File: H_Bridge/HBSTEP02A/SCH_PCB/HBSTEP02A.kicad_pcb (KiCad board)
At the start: 2 copper layers, 0 parts

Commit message: nakresleno schema. Vygenerovan netlist a zalozen PCB.
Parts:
- added C1: 4u7, Capacitors_SMD:C_0805, F.Cu at (188.0, 92.0)
- added C10: 22n, Capacitors_SMD:C_0805, F.Cu at (187.1, 110.9)
- added C11: 100nF, Capacitors_SMD:C_0805, F.Cu at (192.0, 107.3)
- added C12: 470nF, Capacitors_SMD:C_0805, F.Cu at (196.8, 113.6)
- added C13: 100nF, Capacitors_SMD:C_0805, F.Cu at (183.6, 123.5)
- added C14: 100nF, Capacitors_SMD:C_0805, F.Cu at (202.3, 107.3)
- added C15: 470pF, Capacitors_SMD:C_0805, F.Cu at (191.7, 113.6)
- added C16: 470pF, Capacitors_SMD:C_0805, F.Cu at (197.1, 107.3)
- added C17: 470pF, Capacitors_SMD:C_0805, F.Cu at (186.1, 117.2)
- added C18: 470pF, Capacitors_SMD:C_0805, F.Cu at (202.6, 101.0)
- added C19: 4n7, Capacitors_SMD:C_0805, F.Cu at (179.0, 121.3)
- added C2: 100nF, Capacitors_SMD:C_0805, F.Cu at (202.2, 81.6)
- added C20: 4n7, Capacitors_SMD:C_0805, F.Cu at (204.9, 94.2)
- added C21: 4n7, Capacitors_SMD:C_0805, F.Cu at (190.7, 119.9)
- added C22: 4n7, Capacitors_SMD:C_0805, F.Cu at (195.4, 88.4)
- added C3: 100nF, Capacitors_SMD:C_0805, F.Cu at (200.0, 88.4)
- added C4: 100nF, Capacitors_SMD:C_0805, F.Cu at (188.5, 98.3)
- added C5: 100nF, Capacitors_SMD:C_0805, F.Cu at (178.8, 108.0)
- added C6: 4u7, Capacitors_SMD:C_0805, F.Cu at (170.1, 114.8)
- added C7: 100uF/50V, Capacitors_ThroughHole:C_Radial_D10_L13_P5, F.Cu at (161.2, 75.3)
- added C8: 1nF, Capacitors_SMD:C_0805, F.Cu at (164.0, 125.0)
- added C9: 1nF, Capacitors_SMD:C_0805, F.Cu at (174.1, 114.8)
- added D1: M4, Diodes_SMD:SMA_Handsoldering, F.Cu at (136.7, 122.2)
- added D2: MSS1P6, HBSTEP02A:SCHOT_D_MSS1P6, F.Cu at (173.0, 108.7)
- added D3: MSS1P6, HBSTEP02A:SCHOT_D_MSS1P6, F.Cu at (166.5, 108.7)
- added D4: MSS1P6, HBSTEP02A:SCHOT_D_MSS1P6, F.Cu at (158.7, 123.4)
- added D5: MSS1P6, HBSTEP02A:SCHOT_D_MSS1P6, F.Cu at (178.8, 101.9)
- added J1: VIO 3.3-5V, Mlab_Pin_Headers:Straight_2x03, F.Cu at (125.3, 114.4)
- added J10: SDO/NAO/CFG0, Mlab_Pin_Headers:Straight_1x02, F.Cu at (130.9, 73.2)
- added J11: ENCN/DCO, Mlab_Pin_Headers:Straight_1x02, F.Cu at (156.1, 98.3)
- added J12: ENCB/DCEN/CFG4, Mlab_Pin_Headers:Straight_1x02, F.Cu at (111.1, 73.2)
- added J13: ENCA/DCIN/CFG5, Mlab_Pin_Headers:Straight_1x02, F.Cu at (110.7, 83.6)
- added J14: SWP/DIAG1, Mlab_Pin_Headers:Straight_1x02, F.Cu at (138.5, 113.1)
- added J15: SWN/DIAG0, Mlab_Pin_Headers:Straight_1x02, F.Cu at (162.9, 87.9)
- added J16: CONN1_1, Mlab_Con:WAGO256, F.Cu at (108.2, 99.8)
- added J17: CONN1_1, Mlab_Con:WAGO256, F.Cu at (128.6, 81.1)
- added J18: POWER SELECT, Mlab_Pin_Headers:Straight_1x03, F.Cu at (127.2, 101.4)
- added J19: SDMODE, Mlab_Pin_Headers:Straight_1x02, F.Cu at (181.1, 94.0)
- added J2: REFL/STEP, Mlab_Pin_Headers:Straight_1x02, F.Cu at (175.6, 73.2)
- added J20: DRV_ENN_CFG6, Mlab_Pin_Headers:Straight_1x02, F.Cu at (147.6, 83.6)
- added J21: SWSEL, Mlab_Pin_Headers:Straight_1x02, F.Cu at (203.0, 73.2)
- added J22: SPIMODE, Mlab_Pin_Headers:Straight_1x02, F.Cu at (150.3, 120.3)
- added J23: AIN, Mlab_Pin_Headers:Straight_1x02, F.Cu at (161.0, 109.8)
- added J24: CONN1_1, Mlab_Con:WAGO256, F.Cu at (147.8, 70.7)
- added J25: CONN1_1, Mlab_Con:WAGO256, F.Cu at (108.2, 91.5)
- added J3: REFR/DIR, Mlab_Pin_Headers:Straight_1x02, F.Cu at (187.6, 83.6)
- added J4: CLK, Mlab_Pin_Headers:Straight_1x02, F.Cu at (196.7, 73.2)
- added J5: CONN1_1, Mlab_Con:WAGO256, F.Cu at (108.2, 108.0)
- added J6: CONN1_1, Mlab_Con:WAGO256, F.Cu at (128.6, 89.4)
- added J7: CSN/CFG3, Mlab_Pin_Headers:Straight_1x02, F.Cu at (175.7, 83.6)
- added J8: SCK/CFG2, Mlab_Pin_Headers:Straight_1x02, F.Cu at (188.2, 73.2)
- added J9: SID/NAI/CFG1, Mlab_Pin_Headers:Straight_1x02, F.Cu at (108.8, 118.8)
- added L1: 100nH, HBSTEP02A:Inductor_4.5_4.1, F.Cu at (172.4, 104.6)
- added L2: 100nH, HBSTEP02A:Inductor_4.5_4.1, F.Cu at (158.6, 119.3)
- added L3: 100nH, HBSTEP02A:Inductor_4.5_4.1, F.Cu at (196.5, 82.7)
- added L4: 100nH, HBSTEP02A:Inductor_4.5_4.1, F.Cu at (164.9, 119.3)
- added M1: HOLE, Mlab_Mechanical:MountingHole_3mm, F.Cu at (155.3, 109.4)
- added M2: HOLE, Mlab_Mechanical:MountingHole_3mm, F.Cu at (165.9, 99.0)
- added M3: HOLE, Mlab_Mechanical:MountingHole_3mm, F.Cu at (148.5, 109.4)
- added M4: HOLE, Mlab_Mechanical:MountingHole_3mm, F.Cu at (172.9, 94.7)
- added R1: 1k, Resistors_SMD:R_0805, F.Cu at (198.2, 101.0)
- added R10: 0R27, Resistors_SMD:R_1206_HandSoldering, F.Cu at (120.6, 124.2)
- added R11: 10k, Resistors_SMD:R_0805, F.Cu at (204.4, 87.9)
- added R12: 27, Resistors_SMD:R_0805, F.Cu at (187.5, 104.6)
- added R13: 27, Resistors_SMD:R_0805, F.Cu at (167.8, 125.0)
- added R14: 27, Resistors_SMD:R_0805, F.Cu at (178.0, 114.8)
- added R15: 27, Resistors_SMD:R_0805, F.Cu at (183.2, 108.7)
- added R2: 0R27, Resistors_SMD:R_1206_HandSoldering, F.Cu at (127.7, 124.2)
- added R3: 10k, Resistors_SMD:R_0805, F.Cu at (143.2, 121.4)
- added R4: 10k, Resistors_SMD:R_0805, F.Cu at (181.6, 115.0)
- added R5: 22k, Resistors_SMD:R_0805, F.Cu at (201.0, 94.7)
- added R6: 22k, Resistors_SMD:R_0805, F.Cu at (175.1, 121.1)
- added R7: 3.3, Resistors_SMD:R_0805, F.Cu at (171.5, 121.1)
- added R8: _R, Resistors_SMD:R_0805_HandSoldering, F.Cu at (193.7, 101.0)
- added R9: 10k, Resistors_SMD:R_0805, F.Cu at (183.9, 102.4)
- added U1: TMC5130A, Housings_QFP:TQFP-48-1EP_7x7mm_Pitch0.5mm, F.Cu at (144.4, 95.8)
- added VR1: VR, Capacitors_SMD:C_0805, F.Cu at (197.2, 94.7)
- added VR2: VR, Capacitors_SMD:C_0805, F.Cu at (193.1, 94.7)

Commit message: prvni cast pcb
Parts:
- C1, C10, C11, C12, C13, C14, C15, C16, C17, C18, C19, C2, C20, C21, C22, C3, C4, C5, C6, C8, C9, D1, D2, D3, D4, D5, L1, L2, L3, L4, R1, R10, R11, R12, R13, R14, R15, R2, R3, R4, R5, R6, R7, R8, R9, U1, VR1, VR2: moved to B.Cu
- moved J4 102.0 mm to (121.8, 142.4), turned to 180 degrees
- moved J8 99.5 mm to (116.7, 142.4), turned to 180 degrees
- moved J3 94.9 mm to (102.2, 125.1), turned to 90 degrees
- moved C3 93.7 mm to (110.6, 116.6), turned to 90 degrees
- moved C2 93.6 mm to (110.5, 100.1)
- moved J2 91.4 mm to (102.2, 127.6), turned to 90 degrees
- moved R1 85.1 mm to (120.0, 134.6)
- moved R5 83.3 mm to (121.3, 118.7), turned to 180 degrees
- moved C4 83.1 mm to (105.5, 101.9), turned to 90 degrees
- moved J7 81.5 mm to (119.3, 142.4)
- moved C14 81.4 mm to (120.9, 108.6), turned to 90 degrees
- moved C20 80.9 mm to (124.2, 99.8)
- moved C1 78.2 mm to (110.5, 102.6)
- moved C7 75.6 mm to (109.1, 130.2), turned to 270 degrees
- moved VR1 75.3 mm to (133.3, 134.6)
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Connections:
- C21 pad 1: Net-(C21-Pad1) -> GNDA
- C21 pad 2: Net-(C15-Pad2) -> Net-(C21-Pad2)
- C22 pad 1: Net-(C22-Pad1) -> GNDA
- C22 pad 2: Net-(C18-Pad2) -> Net-(C22-Pad2)
- R14 pad 1: GNDA -> Net-(C21-Pad2)
- R14 pad 2: Net-(C21-Pad1) -> Net-(C15-Pad2)
- R15 pad 1: GNDA -> Net-(C22-Pad2)
- R15 pad 2: Net-(C22-Pad1) -> Net-(C18-Pad2)
- U1 pad 49: (no net) -> GNDA
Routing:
- net GNDA: track 0.00 -> 60.3 mm, vias 0 -> 2
- net Net-(J10-Pad1): track 0.00 -> 43.0 mm, vias 0 -> 2
- net VSS: track 0.00 -> 32.6 mm
- net Net-(C9-Pad1): track 0.00 -> 31.0 mm
- net Net-(C8-Pad1): track 0.00 -> 27.0 mm
- net Net-(J23-Pad1): track 0.00 -> 24.9 mm
- net Net-(J20-Pad1): track 0.00 -> 22.0 mm
- net Net-(J15-Pad1): track 0.00 -> 20.5 mm
- net Net-(J13-Pad1): track 0.00 -> 20.0 mm
- net Net-(J21-Pad1): track 0.00 -> 19.7 mm
- net Net-(C15-Pad2): track 0.00 -> 19.7 mm
- net Net-(J14-Pad1): track 0.00 -> 18.7 mm
- net Net-(J9-Pad1): track 0.00 -> 18.6 mm
- net Net-(C11-Pad1): track 0.00 -> 17.5 mm
- net Net-(C16-Pad1): track 0.00 -> 16.4 mm
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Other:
- board outline added: 61 x 61 mm
- net class Default: trace_width 0.25 -> 0.2; via_drill 0.4 -> 0.3
- rule via_min_size: 0.4 -> 0.6

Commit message: layout update
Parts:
- U1: footprint Housings_QFP:TQFP-48-1EP_7x7mm_Pitch0.5mm -> be3D TSSOP:TQFP-48-1EP_7x7mm_Pitch0.5mm_TRINAMIC
- moved C14 24.5 mm to (143.8, 100.0)
- moved R10 23.5 mm to (146.9, 101.6)
- moved J19 15.7 mm to (120.2, 96.2), turned to 0 degrees
- moved J22 15.4 mm to (122.7, 96.2), turned to 0 degrees
- moved C18 7.02 mm to (142.0, 104.1)
- moved L3 6.72 mm to (125.7, 110.0), turned to 270 degrees
- moved L4 6.26 mm to (136.5, 110.0), turned to 270 degrees
- moved C13 6.02 mm to (143.9, 138.7)
- moved C15 5.85 mm to (123.8, 135.3)
- moved C17 5.79 mm to (123.8, 103.9)
- moved D1 5.28 mm to (116.1, 105.5)
- moved R1 4.96 mm to (123.2, 138.4), turned to 90 degrees
- moved D4 4.60 mm to (132.7, 112.0), turned to 270 degrees
- moved C16 4.49 mm to (142.9, 135.3)
- moved R15 4.44 mm to (137.8, 103.9)
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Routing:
- net VSS: track 32.6 -> 112.6 mm, vias 0 -> 2
- net VCOM: track 13.5 -> 90.0 mm, vias 1 -> 3
- net +5V: track 4.04 -> 70.5 mm, vias 0 -> 1
- net VCC: track 6.26 -> 62.2 mm
- net Net-(C14-Pad1): track 0.00 -> 33.7 mm
- net Net-(C13-Pad1): track 6.83 -> 29.8 mm
- net Net-(J4-Pad1): track 12.6 -> 35.3 mm, vias 0 -> 2
- net Net-(J8-Pad1): track 12.9 -> 34.1 mm, vias 0 -> 2
- net Net-(J7-Pad1): track 14.0 -> 33.7 mm, vias 0 -> 2
- net Net-(C15-Pad2): track 19.7 -> 0.00 mm
- net Net-(J22-Pad2): track 6.54 -> 25.5 mm
- net Net-(J19-Pad2): track 7.38 -> 26.0 mm
- net Net-(J9-Pad1): track 18.6 -> 37.0 mm, vias 0 -> 2
- net Net-(C16-Pad1): track 16.4 -> 0.00 mm
- net Net-(J11-Pad1): track 11.9 -> 21.9 mm
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- added copper zone on B.Cu, net +5V
- added copper zone on B.Cu, net GNDA
- added copper zone on F.Cu, net GNDA
- added copper zone on B.Cu, net Net-(C13-Pad1)
- added copper zone on B.Cu, net Net-(C14-Pad1)
- added copper zone on B.Cu, net Net-(C15-Pad2)
- added copper zone on B.Cu, net Net-(C16-Pad1)
- added copper zone on B.Cu, net Net-(C17-Pad2)
- added copper zone on B.Cu, net Net-(C18-Pad2)
- added copper zone on B.Cu, net Net-(D2-Pad1)
- added copper zone on B.Cu, net Net-(D3-Pad1)
- added copper zone on B.Cu, net Net-(D4-Pad1)
- added copper zone on B.Cu, net Net-(D5-Pad1)
- added copper zone on B.Cu, net VCOM
- added copper zone on F.Cu, net VSS
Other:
- board text added: "AIN"
- board text added: "CLK"
- board text added: "CSN/CFG3"
- board text added: "DRV/ENN/CFG6"
- board text added: "ENCA/DCIN/CFG5"
- board text added: "ENCB/DCEN/CFG4"
- board text added: "ENCN/DCO"
- board text added: "MOTOR"
- board text added: "OUT1A"
- board text added: "OUT1B"
- board text added: "OUT2A"
- board text added: "OUT2B"
- board text added: "POW. SEL"
- board text added: "POWER"
- board text added: "REFL/STEP"
- board text added: "REFR/DIR"
- board text added: "SCK/CFG2"
- board text added: "SD MODE"
- board text added: "SDI/NAI/CFG1"
- board text added: "SDO/NAO/CFG0"
- board text added: "SPI MODE"
- board text added: "SWN/DIAG0"
- board text added: "SWP/DIAG0"
- board text added: "SWSEL"

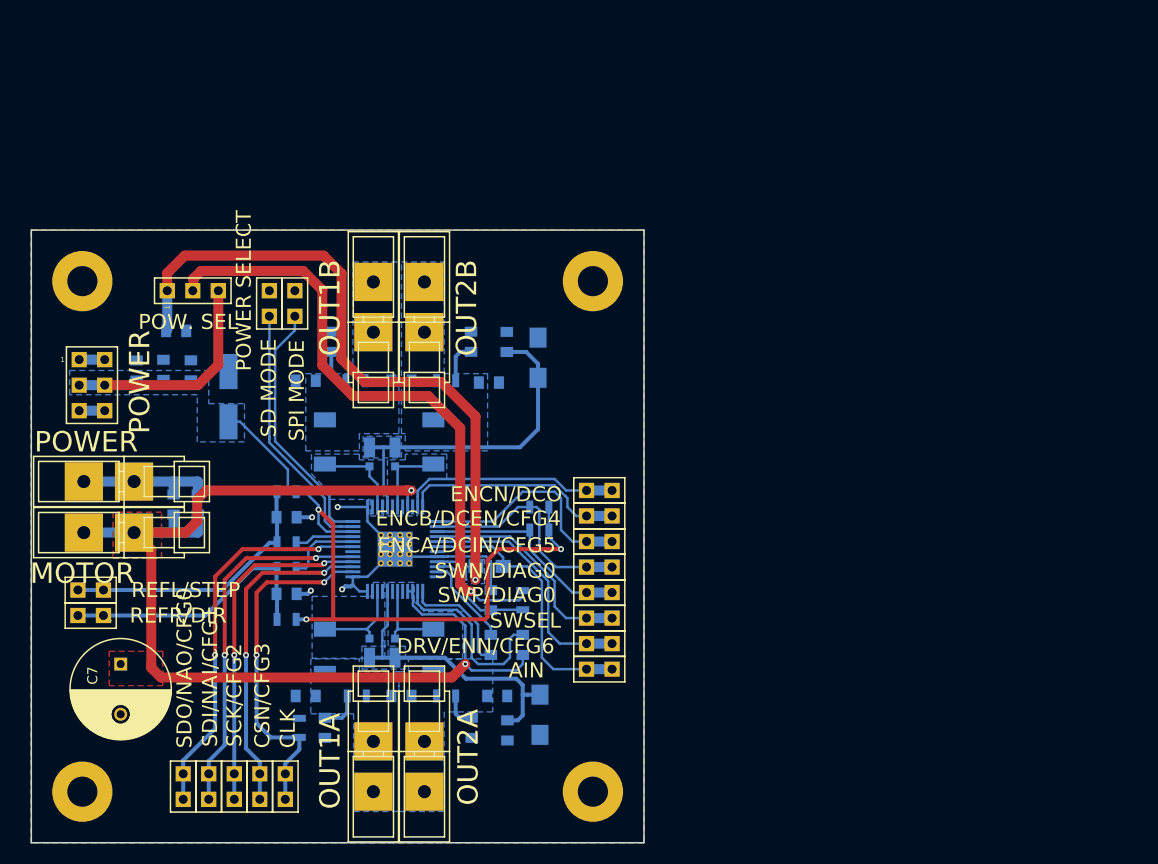
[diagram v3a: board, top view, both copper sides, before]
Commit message: Vylepseni layoutu, popisku a vygenerovani vyrobnich podkladu.
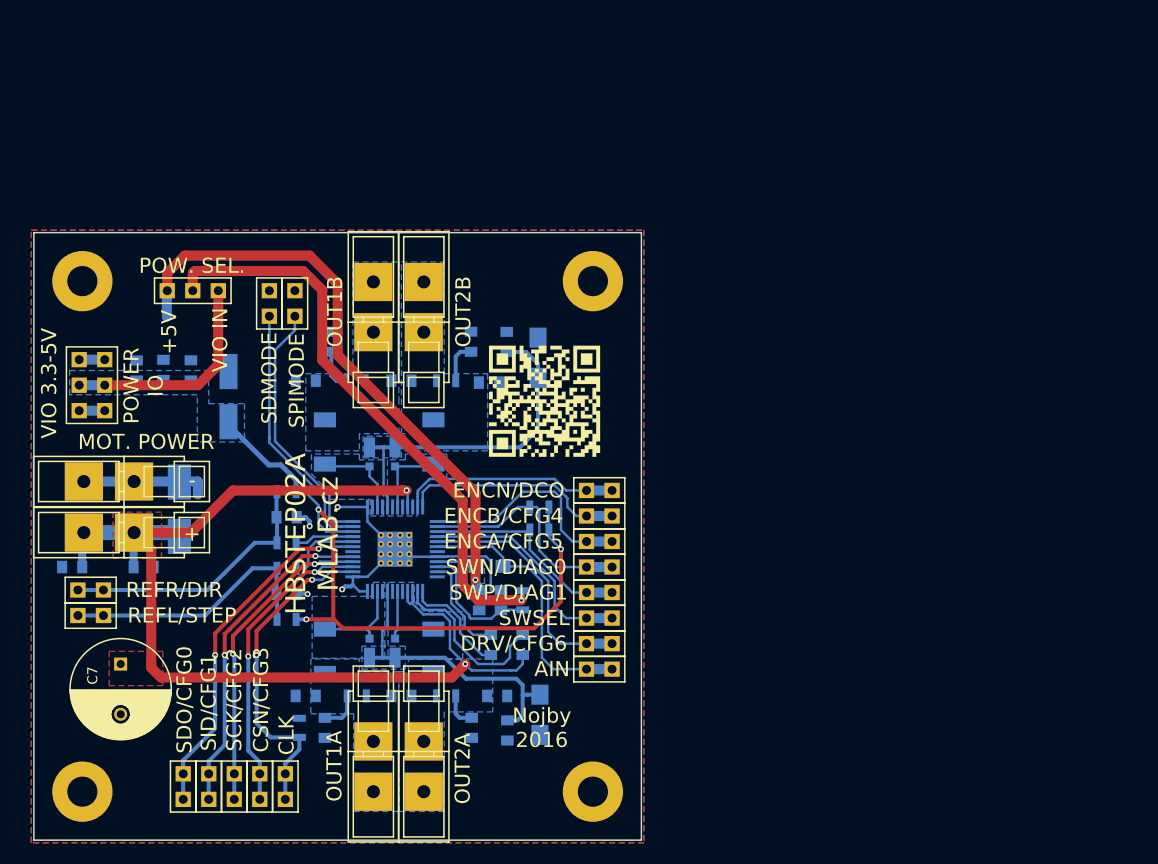
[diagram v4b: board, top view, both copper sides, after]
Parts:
- added D6: M4, Diodes_SMD:SMB_Handsoldering, B.Cu at (111.3, 116.7)
- added G***: LOGO, HBSTEP02A:QR_code, F.Cu at (147.6, 105.9)
- J10: value SDO/NAO/CFG0 -> SDO/CFG0
- J12: value ENCB/DCEN/CFG4 -> ENCB/CFG4
- J13: value ENCA/DCIN/CFG5 -> ENCA/CFG5
- J18: value POWER SELECT -> POW. SEL.
- J20: value DRV_ENN_CFG6 -> DRV/CFG6
- J9: value SID/NAI/CFG1 -> SID/CFG1
- moved C6 40.3 mm to (141.1, 125.7), turned to 270 degrees
- moved C3 11.9 mm to (100.6, 122.4), turned to 180 degrees
- moved C5 8.24 mm to (107.7, 122.4), turned to 0 degrees
- moved C12 1.02 mm to (143.3, 125.7)
- moved J17 0.06 mm to (135.6, 142.3)
- moved J25 0.06 mm to (135.6, 96.5)
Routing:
- net +5V: track 70.5 -> 64.9 mm
- net VCC: track 62.2 -> 58.1 mm
- net Net-(J10-Pad1): track 38.4 -> 35.1 mm
- net Net-(J9-Pad1): track 37.0 -> 33.9 mm
- net Net-(J8-Pad1): track 34.1 -> 31.3 mm
- net Net-(J7-Pad1): track 33.7 -> 31.0 mm
- net Net-(J4-Pad1): track 35.3 -> 33.1 mm
- net Net-(C12-Pad1): track 11.1 -> 12.9 mm
- net Net-(C11-Pad1): track 18.5 -> 17.3 mm
- net Net-(C10-Pad1): track 9.07 -> 10.1 mm
- net Net-(C10-Pad2): track 11.6 -> 10.8 mm
- net VCOM: track 90.0 -> 90.6 mm
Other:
- board size 61 x 61 mm -> 60.5 x 60.5 mm
- board text added: "+"
- board text added: "+5V"
- board text added: "-"
- board text added: "HBSTEP02A MLAB.cz"
- board text added: "MOT. POWER"
- board text added: "Nojby 2016"
- board text added: "POWER IO"
- board text added: "VIO IN"
- board text removed: "AIN"
- board text removed: "CLK"
- board text removed: "CSN/CFG3"
- board text removed: "DRV/ENN/CFG6"
- board text removed: "ENCA/DCIN/CFG5"
- board text removed: "ENCB/DCEN/CFG4"
- board text removed: "ENCN/DCO"
- board text removed: "MOTOR"
- board text removed: "POW. SEL"
- board text removed: "POWER"
- board text removed: "REFL/STEP"
- board text removed: "REFR/DIR"
- board text removed: "SCK/CFG2"
- board text removed: "SD MODE"
- board text removed: "SDI/NAI/CFG1"
- board text removed: "SDO/NAO/CFG0"
- board text removed: "SPI MODE"
- board text removed: "SWN/DIAG0"
- board text removed: "SWP/DIAG0"
- board text removed: "SWSEL"
